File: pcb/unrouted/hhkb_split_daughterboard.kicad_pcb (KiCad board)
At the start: 2 copper layers, 21 x 32 mm, 10 parts

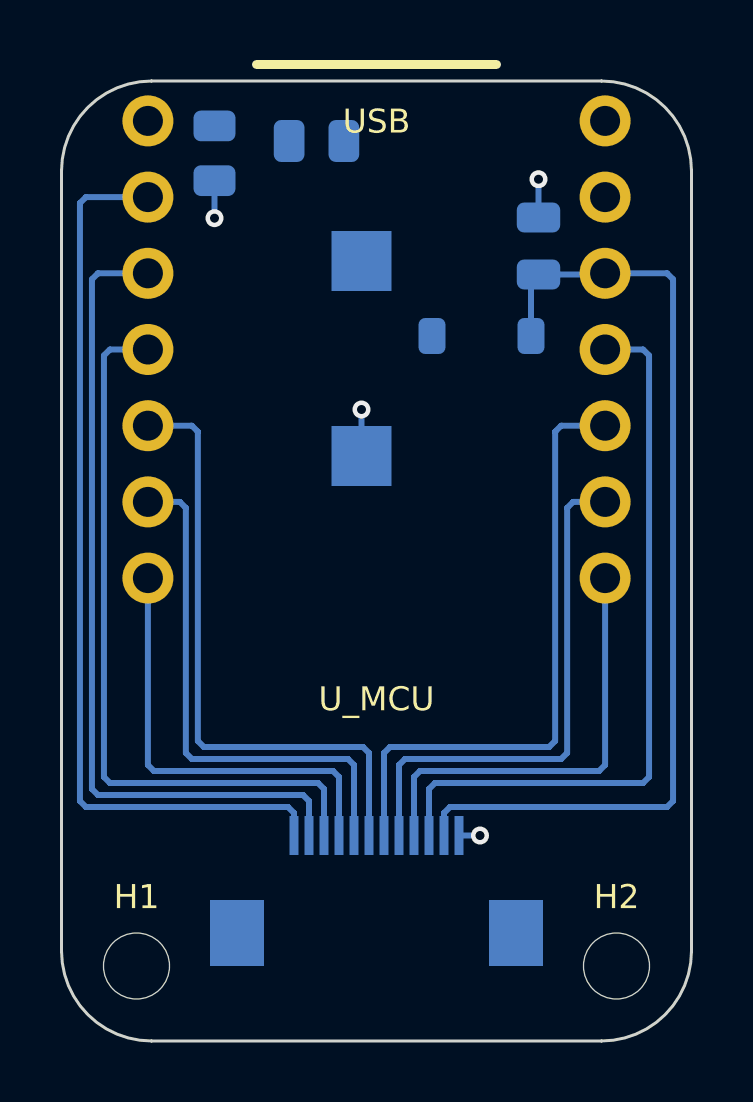
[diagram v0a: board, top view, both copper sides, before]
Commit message: バルク削除後の DB 電源部の配置をスクリプトへ読み戻した（#44）
利用者が KiCad で電源部を寄せ直したものを、gen_daughterboard.py の
POWER_PLACE / SILK_REF へ読み直した。**再生成で部品位置は完全一致する。**

  R_LO   (-5.40, 13.59) → (-5.35, 13.7675)
  R_HI   (-2.00, 14.00) → (-2.01, 14.68)
  SW_PWR (-0.50, 10.00) → (-0.68, 12.20)
  D_PWR  ( 3.50,  7.50) → ( 1.51,  9.55)   旧 C_BULK の跡地の側へ
  C_DB                    動いていない

シルクは _read_silk_from で吸い出した（手で書き写していない）。

⚠️ R_LO のシルクだけ利用者の値と違う (1.4475,-1.390) → (2.900,0.000)。
利用者のファイルはゾーンを塗り直していないので DRC が別の 21 件で
埋まっていて、ラベルが自分の外形線まで 0.0823mm（要 0.15mm）という
1 件が隠れていた。自分の外形線と R_HI のラベルに挟まれていて左右へは
逃がせないので手前へ出した。R_LO は Flip されていて dy の符号が
反転する点に注意（理由は表の脇に記録）。

再生成した子基板は 違反 0 / 未配線 0 / 警告 0。

なお pytest tools の赤 5 件は HEAD の綺麗なワークツリーで再現を確認済みで、
すべてこの変更より前からのもの（right の未配線・single_pin・記録の鮮度）。
うち pcb_parts.json の鮮度は 3 基板とも前から古く、直すと left/right を
巻き込むため今回は触っていない。

Co-Authored-By: Claude Opus 5 (1M context) <noreply@anthropic.com>
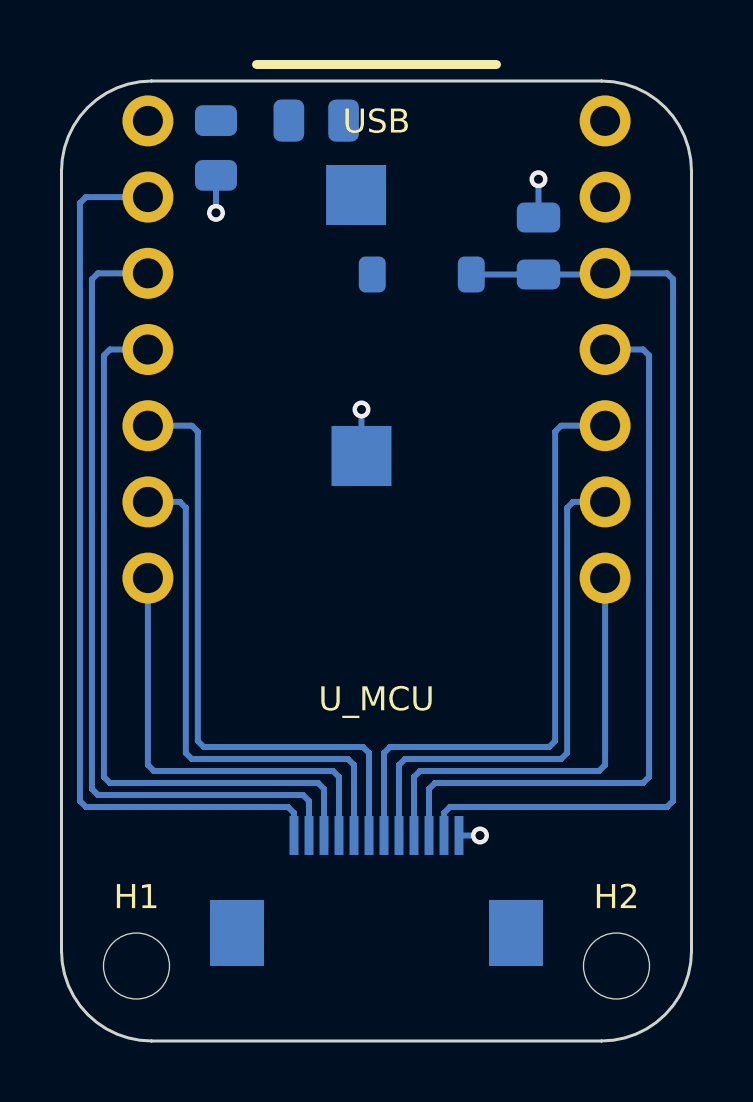
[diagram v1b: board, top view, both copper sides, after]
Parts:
- moved D_PWR 2.86 mm to (151.5, 90.5)
- moved SW_PWR_1 2.21 mm to (149.3, 87.8)
- moved R_HI 0.68 mm to (148.0, 85.3)
- moved R_LO 0.18 mm to (144.7, 86.2)

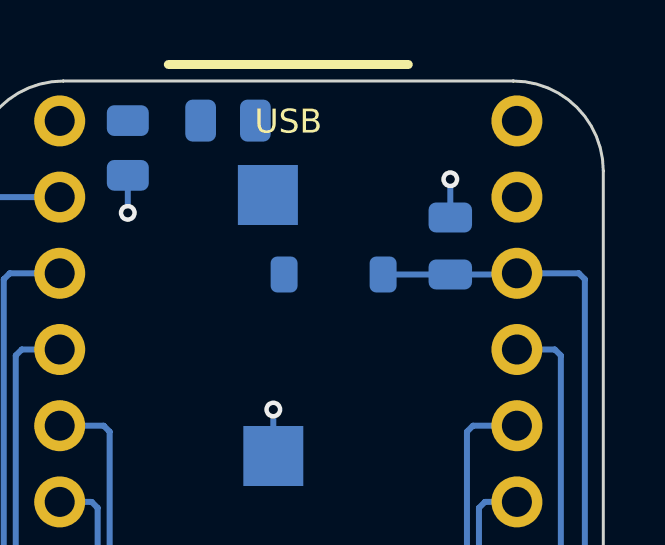
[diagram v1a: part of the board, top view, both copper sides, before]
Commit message: C_DB を消した（負荷の直近にいないパスコンだった・#45）
子基板のパスコン C_DB（0.1µF・C49678）を削除した。実装部品が 2 個減る
（左右に 1 個ずつ）。#44 と合わせて、子基板のコンデンサは 0 個になった。

**理由は「相手がいない」ではなく「取り分が誤差」。**3V3 の負荷は最初から
2 つあり、どちらも子基板の外にいた:

  nRF52840 → XIAO の内部。内蔵の 2.2µF ×5 が桁違いに近い
  595 ×2   → 主基板。直近の C_U1/C_U2 が 58:1 で取る

電流は近い順ではなく、ループインダクタンスに反比例して分流する。
足りているところに数 % を足しても改善せず、不足していたなら数 % では
救えない。どちらに転んでも出番が無い。

LDO（SGM2040・型番一致を確認）の安定条件 C_OUT=0.1〜10µF も内部の
公称 11µF が満たす。上限側は既に超えており、外から足す議論は成立しない。

調査文書の結論は独立に再検証してから実行した:

  §1 子基板の 3V3 は 4 パッドで全数  → .kicad_pcb を走査して一致
  §2 XIAO 内部の 2.2µF ×5           → Seeed の KiCad ソース（73 footprint）
                                       を自分で数え直して完全一致
  §3 分流比 58:1                     → 152Ω ÷ 2.6Ω で一致

検査は「C_DB が復活していないこと」ではなく、**その負荷の直近に誰かいるか**
を見る（test_the_daughterboard_has_no_part_that_needs_local_decoupling）。
子基板に 595 を足す／ICS を空にする、の 2 通りで落ちることを確認済み。

ICS から xiao_nrf52840 を外した。XIAO は IC ではなくモジュールで内蔵して
いるため。「XIAO にパスコンが無い」と足し直されないよう理由をコードに残した。

子基板 DRC: 違反 0 / 未配線 0 / 警告 0。回路図は部品 8 → 7 個。

⚠️ 電源部（R_LO/R_HI/SW_PWR/D_PWR）は動かしていない。利用者が KiCad で
釣り合いを取った値で、SILK_REF の余白が 0.15mm ぎりぎりのため。

Co-Authored-By: Claude Opus 5 (1M context) <noreply@anthropic.com>
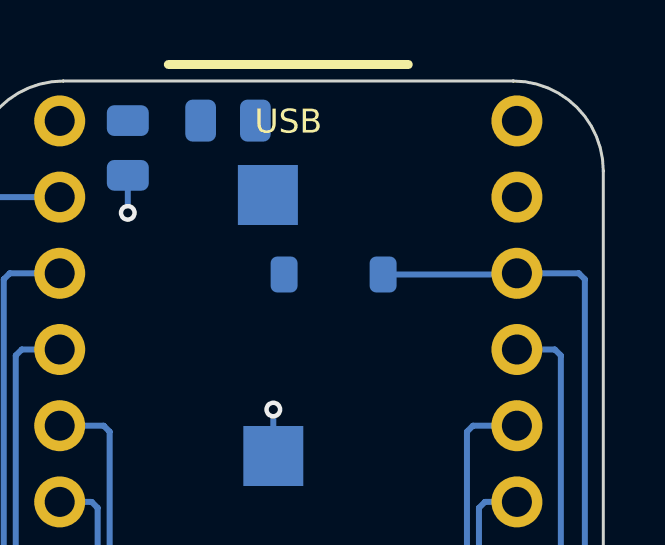
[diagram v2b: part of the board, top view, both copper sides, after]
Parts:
- removed C_DB: 0.1uF, C_0805_2012Metric
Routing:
- net GND: track 4.78 -> 3.50 mm, vias 4 -> 3

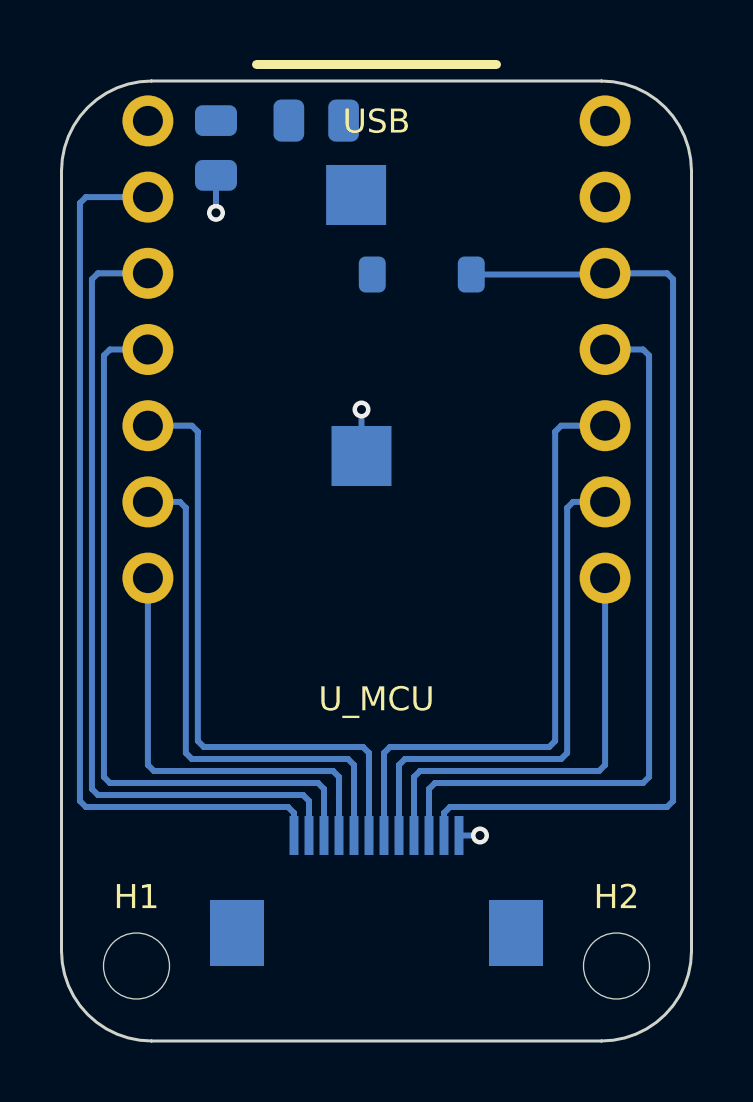
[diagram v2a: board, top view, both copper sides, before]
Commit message: 子基板で利用者が動かした 2 つを生成器へ戻した（BT1_- と SW_PWR_1）
KiCad で直したものが再生成で消えないように、出所を生成器にした。

- BT1_- のランド: POWER_PLACE (-0.50, 3.50) → (4.375, 13.55)
- SW_PWR_1 の参照名: SILK_REF (-3.390, 2.130, 180.0) → (1.320, -4.550, 270.0)

シルクは手で写さず _read_silk_from で吸い出した。gen_daughterboard →
autoroute → drc を回し、生成物と利用者のファイルを機械で突き合わせて
一致を確認（部品 9 個の座標・角度・参照名の位置、パッド 37 個の座標と
ネット、計 46 項目）。DRC は 違反 0 / 未配線 0 / 警告 0。

⚠️ y の符号を ORIGIN=(150,93) と読み違えて一度 7mm ずれた値を入れた。
正しくは ORIGIN=(150,100)。突き合わせで出た。

移動の理由は聞いていないので書いていない（推測で戻さないよう注記だけ）。

test_pcb / test_circuit / test_assembly の 7 件が赤だが、全部 left/right で
この変更より前から赤（stash して同じ 7 件が出ることを確認済み）。

Co-Authored-By: Claude Opus 5 (1M context) <noreply@anthropic.com>
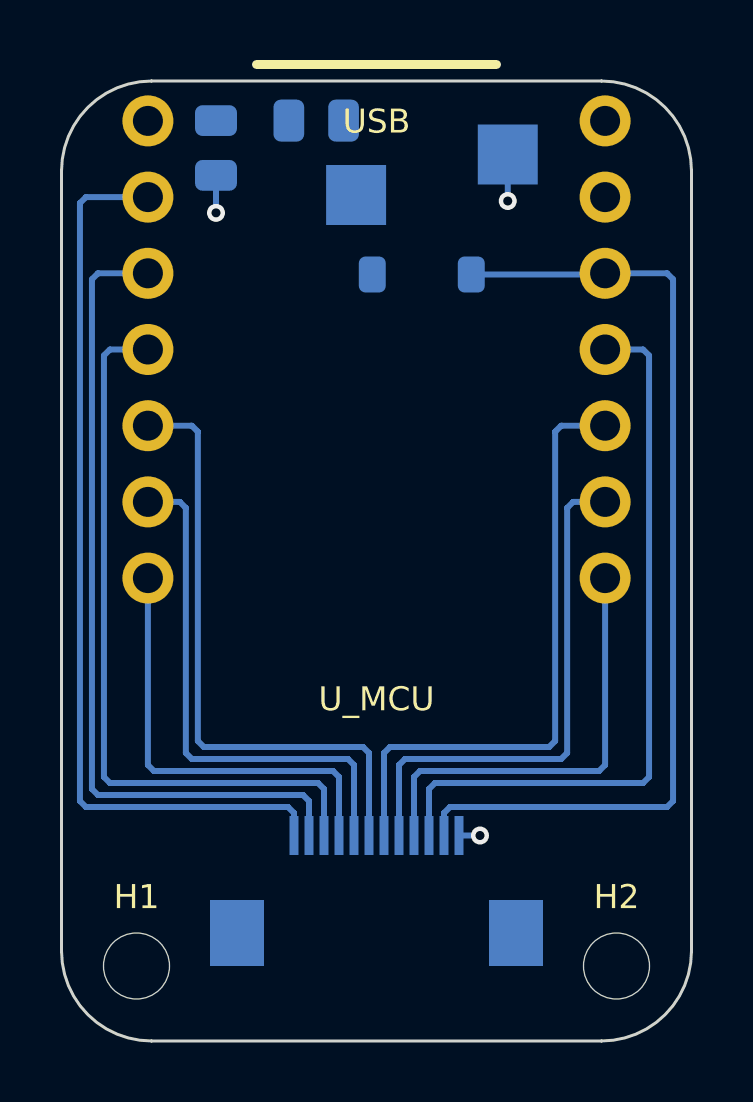
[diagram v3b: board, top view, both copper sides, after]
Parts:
- moved BT1_- 11.2 mm to (154.4, 86.5)
